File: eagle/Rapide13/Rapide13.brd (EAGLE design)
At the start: 50 x 50 mm, 22 parts, among them IC1 AT90S2313P, IC2 TINY13-20PU, IC3 TINY13-20SSU, J1 AVR_SPI_PRG_6PTH

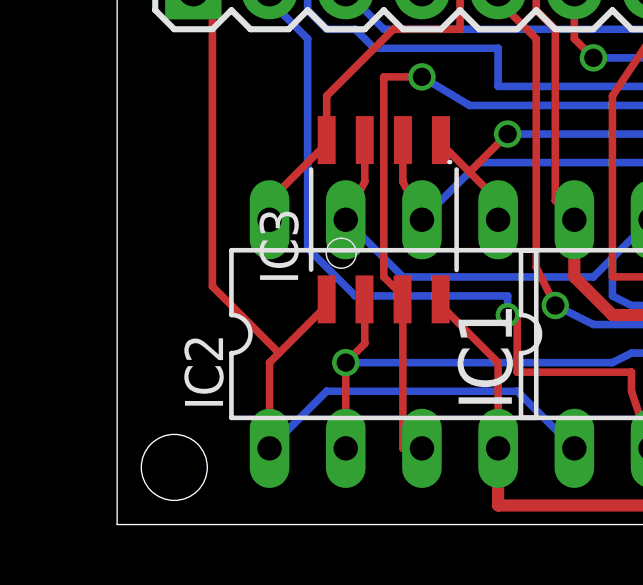
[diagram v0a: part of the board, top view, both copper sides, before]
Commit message: v1.0 sent to production at Seeed
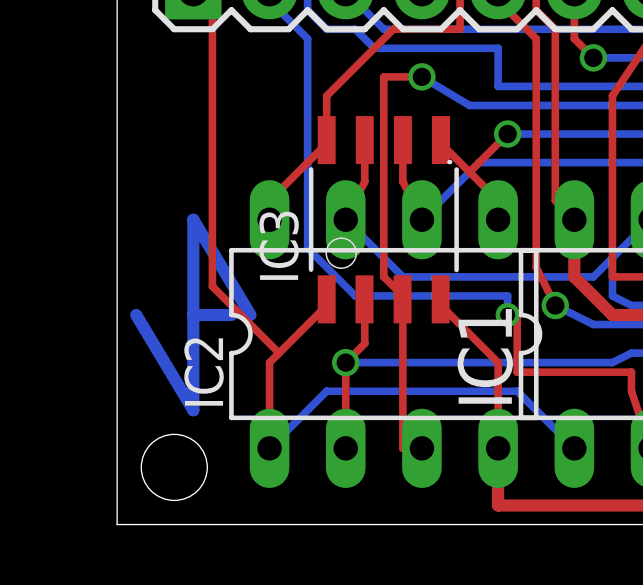
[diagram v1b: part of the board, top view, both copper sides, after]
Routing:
- net N$13: track 0.00 -> 15.0 mm
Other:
- board text added: "Attiny13:"
- board text added: "B0"
- board text added: "B1"
- board text added: "B2"
- board text added: "B3"
- board text added: "B4"
- board text added: "B5"
- board text added: "B5=>B0,B6=>B1"
- board text added: "B6"
- board text added: "B7"
- board text added: "B7=>B2"
- board text added: "D0"
- board text added: "D1"
- board text added: "D2"
- board text added: "D3"
- board text added: "D4"
- board text added: "D5"
- board text added: "D6"
- board text added: "RST"
- board text added: "X1"
- board text added: "X2"
- board text added: "http://kalshagar.wikispaces.com/Rapide13"
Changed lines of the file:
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@@
 <wire x1="50.165" y1="26.67" x2="0" y2="26.67" width="0.4064" layer="48"/>
 <wire x1="0" y1="29.21" x2="50.165" y2="29.21" width="0.4064" layer="48"/>
-<text x="0" y="29.5275" size="1.778" layer="48">+</text>
-<text x="1.27" y="27.6225" size="1.778" layer="48" rot="R90">-</text>
+<text x="0.3175" y="29.5275" size="1.778" layer="48" font="vector">+</text>
+<text x="1.905" y="27.305" size="1.778" layer="48" font="vector" rot="R90">-</text>
 <wire x1="0" y1="22.86" x2="50.165" y2="22.86" width="0.254" layer="48"/>
 <text x="46.99" y="15.875" size="1.016" layer="48">VCC</text>
@@
 <text x="45.4025" y="45.4025" size="1.016" layer="48" rot="R90">RAW</text>
 <rectangle x1="6.35" y1="8.255" x2="6.985" y2="12.065" layer="48"/>
-<text x="8.255" y="4.445" size="1.016" layer="48">Attiny13</text>
-<text x="33.02" y="4.445" size="1.016" layer="48">Attiny2313</text>
-<text x="1.5875" y="3.81" size="1.016" layer="48" rot="R90">Rapide13</text>
-<text x="3.175" y="3.81" size="1.016" layer="48" rot="R90">v1.0 Mar2013</text>
-<wire x1="40.64" y1="2.54" x2="41.91" y2="4.445" width="0.3048" layer="48"/>
-<wire x1="41.91" y1="4.445" x2="41.91" y2="2.54" width="0.3048" layer="48"/>
-<wire x1="41.91" y1="2.54" x2="41.91" y2="0.635" width="0.3048" layer="48"/>
-<wire x1="41.91" y1="0.635" x2="43.18" y2="2.54" width="0.3048" layer="48"/>
-<wire x1="41.91" y1="2.54" x2="40.9575" y2="2.54" width="0.3048" layer="48"/>
+<text x="6.6675" y="4.1275" size="1.016" layer="48" font="vector">Attiny13</text>
+<text x="31.115" y="5.08" size="1.016" layer="48" font="vector">Attiny2313</text>
+<text x="1.5875" y="3.81" size="1.016" layer="48" font="vector" rot="R90">Rapide13</text>
+<text x="1.27" y="33.02" size="1.016" layer="48" font="vector" rot="R90">v1.0 Mar2013</text>
+<text x="3.175" y="13.335" size="1.016" layer="48" font="vector" rot="R90">RST</text>
+<text x="5.715" y="14.2875" size="1.016" layer="48" font="vector" rot="R90">D0</text>
+<text x="8.255" y="14.2875" size="1.016" layer="48" font="vector" rot="R90">D1</text>
+<text x="15.875" y="14.2875" size="1.016" layer="48" font="vector" rot="R90">D2</text>
+<text x="10.795" y="14.2875" size="1.016" layer="48" font="vector" rot="R90">X2</text>
+<text x="13.335" y="14.2875" size="1.016" layer="48" font="vector" rot="R90">X1</text>
+<text x="18.415" y="14.2875" size="1.016" layer="48" font="vector" rot="R90">D3</text>
+<text x="20.955" y="14.2875" size="1.016" layer="48" font="vector" rot="R90">D4</text>
+<text x="23.495" y="14.2875" size="1.016" layer="48" font="vector" rot="R90">D5</text>
+<text x="26.035" y="14.2875" size="1.016" layer="48" font="vector" rot="R90">D6</text>
+<text x="28.575" y="14.2875" size="1.016" layer="48" font="vector" rot="R90">B0</text>
+<text x="31.115" y="14.2875" size="1.016" layer="48" font="vector" rot="R90">B1</text>
+<text x="33.655" y="14.2875" size="1.016" layer="48" font="vector" rot="R90">B2</text>
+<text x="36.195" y="14.2875" size="1.016" layer="48" font="vector" rot="R90">B3</text>
+<text x="38.735" y="14.2875" size="1.016" layer="48" font="vector" rot="R90">B4</text>
+<text x="41.275" y="14.2875" size="1.016" layer="48" font="vector" rot="R90">B5</text>
+<text x="43.815" y="14.2875" size="1.016" layer="48" font="vector" rot="R90">B6</text>
+<text x="46.355" y="14.2875" size="1.016" layer="48" font="vector" rot="R90">B7</text>
+<wire x1="1.905" y1="16.51" x2="1.905" y2="12.7" width="0.254" layer="48"/>
+<wire x1="1.905" y1="12.7" x2="3.81" y2="12.7" width="0.254" layer="48"/>
+<wire x1="3.81" y1="12.7" x2="3.81" y2="15.875" width="0.254" layer="48"/>
+<wire x1="3.81" y1="15.875" x2="3.175" y2="16.51" width="0.254" layer="48"/>
+<wire x1="40.005" y1="16.51" x2="40.005" y2="13.97" width="0.254" layer="48"/>
+<wire x1="40.005" y1="13.97" x2="41.91" y2="13.97" width="0.254" layer="48"/>
+<wire x1="41.91" y1="13.97" x2="41.91" y2="15.875" width="0.254" layer="48"/>
+<wire x1="41.91" y1="15.875" x2="41.275" y2="16.51" width="0.254" layer="48"/>
+<wire x1="34.925" y1="16.51" x2="34.925" y2="13.97" width="0.254" layer="48"/>
+<wire x1="34.925" y1="13.97" x2="36.83" y2="13.97" width="0.254" layer="48"/>
+<wire x1="36.83" y1="13.97" x2="36.83" y2="15.875" width="0.254" layer="48"/>
+<wire x1="36.83" y1="15.875" x2="36.195" y2="16.51" width="0.254" layer="48"/>
+<wire x1="37.465" y1="16.51" x2="37.465" y2="13.97" width="0.254" layer="48"/>
+<wire x1="37.465" y1="13.97" x2="39.37" y2="13.97" width="0.254" layer="48"/>
+<wire x1="39.37" y1="13.97" x2="39.37" y2="15.875" width="0.254" layer="48"/>
+<wire x1="39.37" y1="15.875" x2="38.735" y2="16.51" width="0.254" layer="48"/>
+<wire x1="42.545" y1="16.51" x2="42.545" y2="13.97" width="0.254" layer="48"/>
+<wire x1="42.545" y1="13.97" x2="44.45" y2="13.97" width="0.254" layer="48"/>
+<wire x1="44.45" y1="13.97" x2="44.45" y2="15.875" width="0.254" layer="48"/>
+<wire x1="44.45" y1="15.875" x2="43.815" y2="16.51" width="0.254" layer="48"/>
+<wire x1="45.085" y1="16.51" x2="45.085" y2="13.97" width="0.254" layer="48"/>
+<wire x1="45.085" y1="13.97" x2="46.99" y2="13.97" width="0.254" layer="48"/>
+<wire x1="46.99" y1="13.97" x2="46.99" y2="15.875" width="0.254" layer="48"/>
+<wire x1="46.99" y1="15.875" x2="46.355" y2="16.51" width="0.254" layer="48"/>
+<text x="39.37" y="1.905" size="0.6096" layer="48" font="vector">B5=&gt;B0,B6=&gt;B1</text>
+<text x="39.37" y="0.635" size="0.6096" layer="48" font="vector">B7=&gt;B2</text>
+<text x="40.3225" y="3.175" size="0.6096" layer="48" font="vector">Attiny13:</text>
+<wire x1="39.0525" y1="2.8575" x2="40.64" y2="2.8575" width="0.127" layer="48"/>
+<wire x1="40.64" y1="2.8575" x2="40.64" y2="1.905" width="0.127" layer="48"/>
+<wire x1="40.64" y1="1.905" x2="40.3225" y2="1.5875" width="0.127" layer="48"/>
+<wire x1="40.3225" y1="1.5875" x2="39.0525" y2="1.5875" width="0.127" layer="48"/>
+<wire x1="39.0525" y1="1.5875" x2="39.0525" y2="2.8575" width="0.127" layer="48"/>
+<wire x1="42.8625" y1="2.8575" x2="44.45" y2="2.8575" width="0.127" layer="48"/>
+<wire x1="44.45" y1="2.8575" x2="44.45" y2="1.905" width="0.127" layer="48"/>
+<wire x1="44.45" y1="1.905" x2="44.1325" y2="1.5875" width="0.127" layer="48"/>
+<wire x1="44.1325" y1="1.5875" x2="42.8625" y2="1.5875" width="0.127" layer="48"/>
+<wire x1="42.8625" y1="1.5875" x2="42.8625" y2="2.8575" width="0.127" layer="48"/>
+<wire x1="40.3225" y1="1.5875" x2="40.64" y2="1.5875" width="0.127" layer="48"/>
+<wire x1="40.64" y1="1.5875" x2="40.64" y2="0.635" width="0.127" layer="48"/>
+<wire x1="40.64" y1="0.635" x2="40.3225" y2="0.3175" width="0.127" layer="48"/>
+<wire x1="40.3225" y1="0.3175" x2="39.0525" y2="0.3175" width="0.127" layer="48"/>
+<wire x1="39.0525" y1="0.3175" x2="39.0525" y2="1.5875" width="0.127" layer="48"/>
+<text x="5.08" y="7.9375" size="1.016" layer="48" font="vector">+</text>
+<text x="6.0325" y="12.3825" size="1.016" layer="48" font="vector">+</text>
+<text x="15.24" y="7.9375" size="1.016" layer="48" font="vector">+</text>
+<text x="12.065" y="0.635" size="0.6096" layer="48" font="vector">GND</text>
+<text x="36.83" y="0.635" size="0.6096" layer="48" font="vector">GND</text>
+<rectangle x1="46.99" y1="9.525" x2="49.53" y2="10.16" layer="48"/>
+<text x="1.27" y="41.91" size="0.8128" layer="52" font="vector" rot="MR270">http://kalshagar.wikispaces.com/Rapide13</text>
 </plain>
 <attributes>
@@
 <wire x1="31.115" y1="46.99" x2="31.115" y2="44.7675" width="0.254" layer="1"/>
 </signal>
+<signal name="N$13">
+<wire x1="4.445" y1="6.985" x2="2.54" y2="10.16" width="0.4064" layer="16"/>
+<wire x1="2.54" y1="10.16" x2="2.54" y2="6.985" width="0.4064" layer="16"/>
+<wire x1="2.54" y1="6.985" x2="2.54" y2="3.81" width="0.4064" layer="16"/>
+<wire x1="2.54" y1="3.81" x2="0.635" y2="6.985" width="0.4064" layer="16"/>
+<wire x1="2.54" y1="6.985" x2="3.81" y2="6.985" width="0.4064" layer="16"/>
+</signal>
 </signals>
